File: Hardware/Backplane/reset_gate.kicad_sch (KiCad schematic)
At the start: 1 part, among them U1101 SN74LVC1G08DBVR

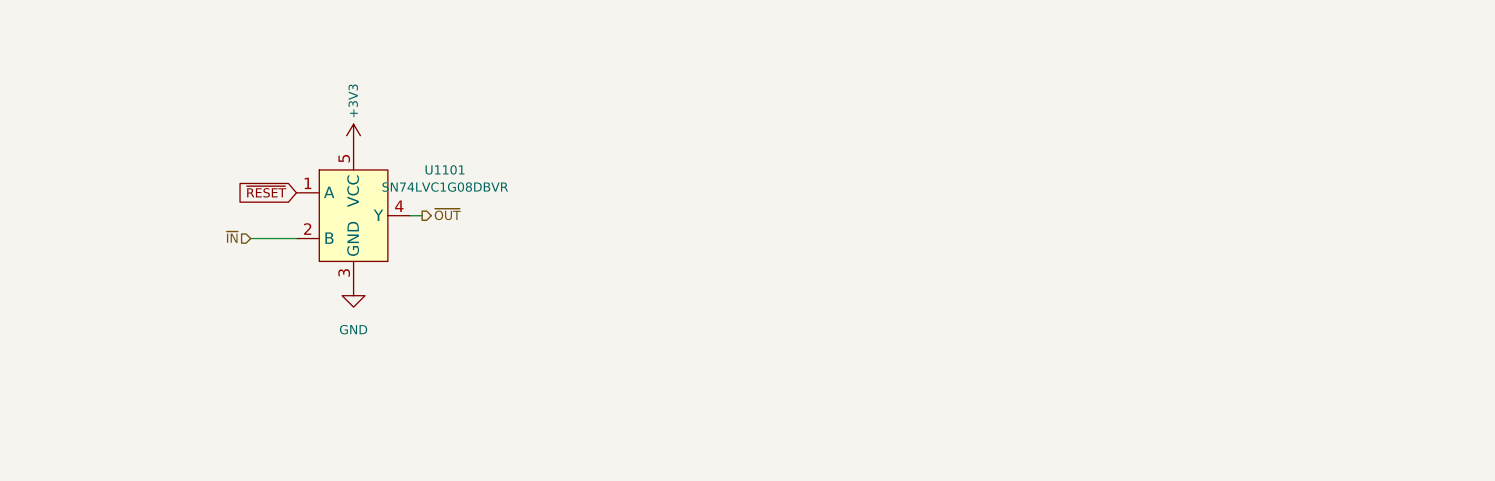
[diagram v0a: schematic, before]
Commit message: Some work on the backplane schematics: Improves module locality
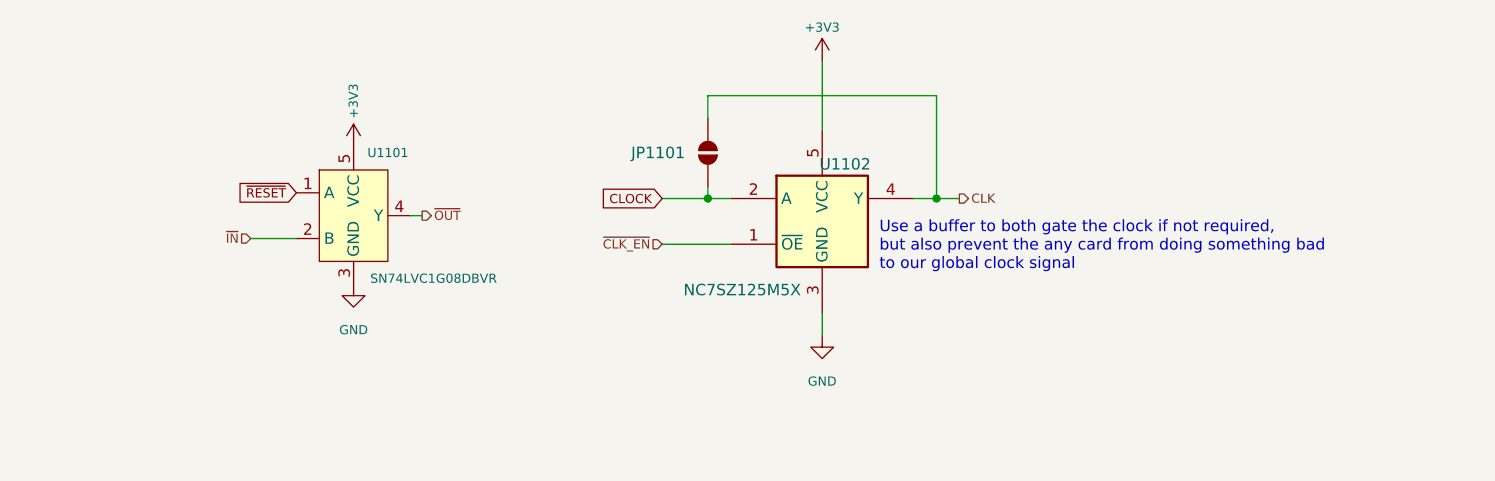
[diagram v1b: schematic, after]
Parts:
- added JP1101: SolderJumper_2_Open, Jumper:SolderJumper-2_P1.3mm_Open_RoundedPad1.0x1.5mm, symbol Jumper:SolderJumper_2_Open
- added U1102: NC7SZ125M5X, Package_TO_SOT_SMD:SOT-23-5, symbol 74xGxx:NC7SZ125M5X
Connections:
- net +3V3: now also U1102.5 (VCC)
- net GND: now also U1102.3 (GND)
- new net CLK: JP1101.2 (B), U1102.4 (Y)
- new net CLOCK: JP1101.1 (A), U1102.2 (A)
- new net ~{CLK_EN}: U1102.1 (~{OE})
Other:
- note added: "Use a buffer to both gate the clock if not required, but also prevent the any card from doing something bad to our global clock signal"

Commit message: Cleans up the backplane schematic and improves on features a lot.
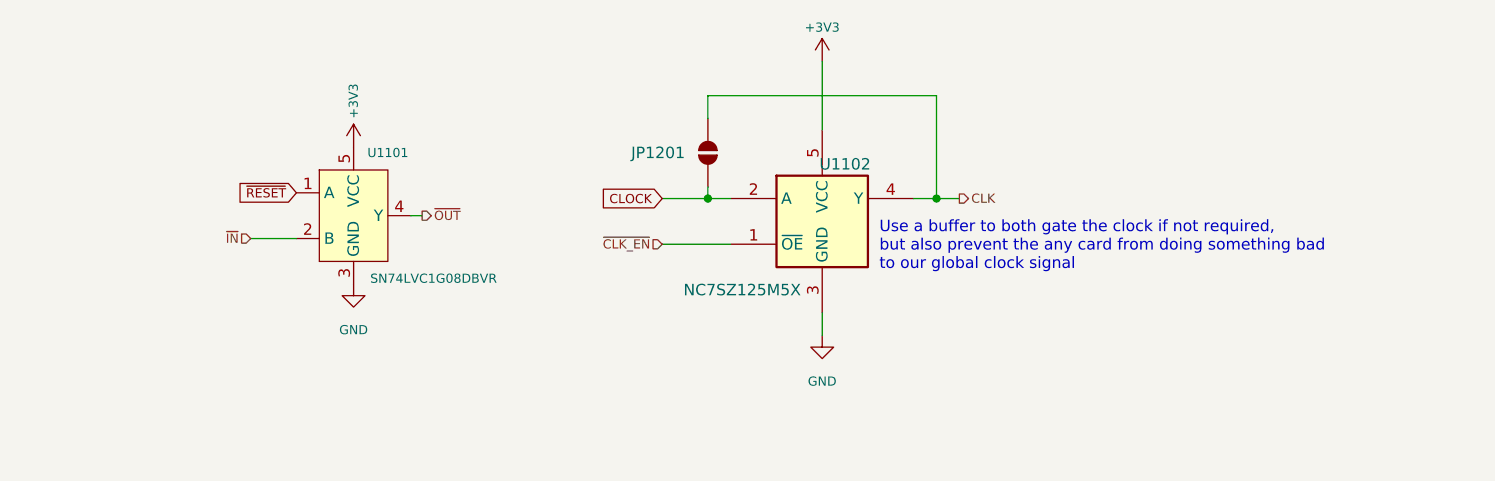
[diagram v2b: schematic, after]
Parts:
- renumbered JP1101 to JP1201
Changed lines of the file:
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@@
 		(on_board yes)
 		(dnp no)
-		(property "Reference" "JP1101"
+		(property "Reference" "JP1201"
 			(at 99.06 35.5599 90)
 			(effects
@@
 		(pin "2"
 		)
-		(instances
-			(project ""
-				(path "/c6da991a-d3ed-4ac1-8b0d-12cd7ba8539b/50c65fc9-71ad-406b-a67c-9fe60e10adc6"
-					(reference "JP1101")
-					(unit 1)
-				)
-				(path "/c6da991a-d3ed-4ac1-8b0d-12cd7ba8539b/1a72b562-b374-42f7-9675-d69ad55f0ee3/0a06f79e-2371-44d6-ba59-f8569181be44"
-					(reference "JP1701")
-					(unit 1)
-				)
-				(path "/c6da991a-d3ed-4ac1-8b0d-12cd7ba8539b/51cd8e93-cd1c-4686-bc6f-5ee712165889/0a06f79e-2371-44d6-ba59-f8569181be44"
-					(reference "JP1501")
-					(unit 1)
-				)
-				(path "/c6da991a-d3ed-4ac1-8b0d-12cd7ba8539b/58d27b07-4dc5-4035-a4cc-e2edbe424767/0a06f79e-2371-44d6-ba59-f8569181be44"
-					(reference "JP1601")
-					(unit 1)
-				)
-				(path "/c6da991a-d3ed-4ac1-8b0d-12cd7ba8539b/75f5bf2b-cae9-41fc-95c9-e5109fcf3957/0a06f79e-2371-44d6-ba59-f8569181be44"
-					(reference "JP1401")
-					(unit 1)
-				)
-				(path "/c6da991a-d3ed-4ac1-8b0d-12cd7ba8539b/de0a9853-8d2d-4021-a172-17dfe1844021/0a06f79e-2371-44d6-ba59-f8569181be44"
-					(reference "JP1801")
-					(unit 1)
-				)
-				(path "/c6da991a-d3ed-4ac1-8b0d-12cd7ba8539b/e09cd553-1ab8-4f68-be82-b6b3b295ca8c/0a06f79e-2371-44d6-ba59-f8569181be44"
-					(reference "JP1201")
-					(unit 1)
-				)
-				(path "/c6da991a-d3ed-4ac1-8b0d-12cd7ba8539b/fc8eca16-66d0-4021-950c-0054f8a34b69/0a06f79e-2371-44d6-ba59-f8569181be44"
-					(reference "JP1301")
-					(unit 1)
-				)
-			)
-		)
 	)

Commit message: Cleans up schematic, adds clean RESET gating
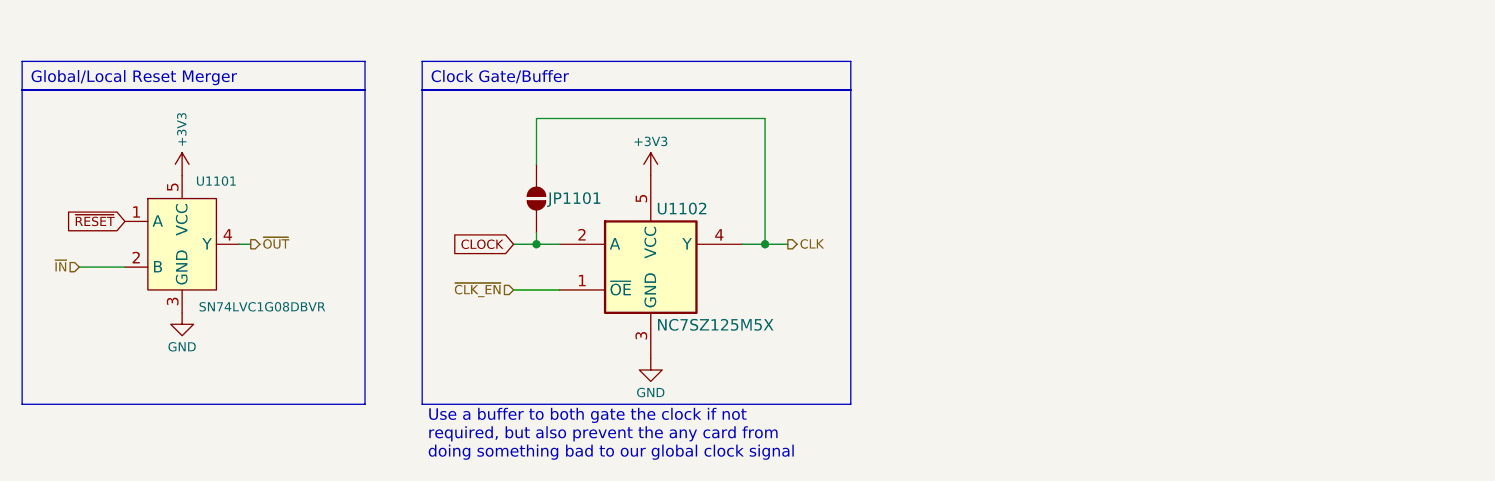
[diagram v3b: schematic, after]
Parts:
- renumbered JP1201 to JP1101
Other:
- company: (none) -> Ashet Technologies
- title: (none) -> Clock and Reset Gate
- moved on the sheet: JP1101, U1101, U1102

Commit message: Refactors clock system to use AND gates for clock tree spanning and gating.
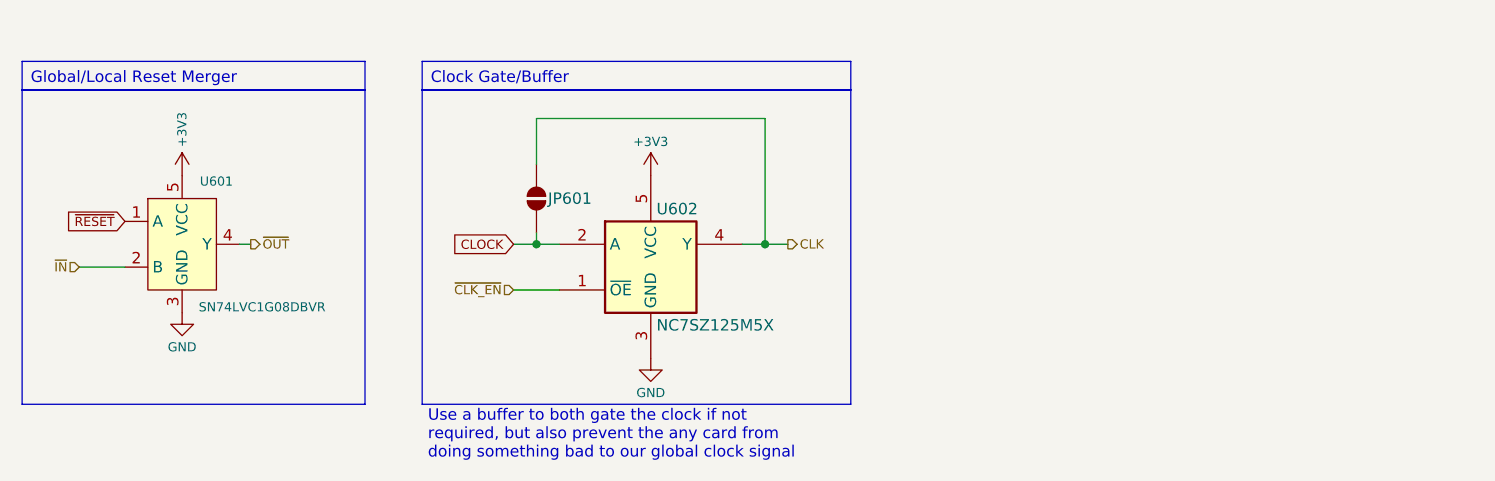
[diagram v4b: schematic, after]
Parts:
- renumbered JP1101 to JP601, U1101 to U601, U1102 to U602
